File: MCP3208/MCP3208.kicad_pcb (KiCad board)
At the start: 2 copper layers, 52.3 x 29.7 mm, 34 parts, among them J1 5V, J2 SPI, J3 CH4, J4 CH3, J5 CH2, J6 CH1, U1 MCP1541, U2 MCP6021, U3 MCP3208

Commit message: PCB layout changes
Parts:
- moved C8 0.80 mm to (108.0, 79.4)
- moved J1 0.64 mm to (127.3, 66.7)
- moved J2 0.64 mm to (127.3, 72.9)
- moved C2 0.25 mm to (117.0, 63.5)
- moved FB1 0.25 mm to (106.3, 66.9)
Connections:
- U2 pad 1: Net-(U2-Pad1) -> (no net)
- U2 pad 5: Net-(U2-Pad5) -> (no net)
- U2 pad 8: Net-(U2-Pad8) -> (no net)
- U3 pad 6: Net-(U3-Pad6) -> (no net)
- U3 pad 7: Net-(U3-Pad7) -> (no net)
- U3 pad 8: Net-(U3-Pad8) -> (no net)
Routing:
- net GND: track 50.8 -> 53.2 mm, vias 19 -> 23
- net /SPI.MISO: track 24.3 -> 25.2 mm
- net /SPI.MOSI: track 23.8 -> 24.7 mm
- net /SPI.CS0: track 23.2 -> 24.2 mm
- net /SPI.CLK: track 24.8 -> 25.8 mm
- net Net-(C8-Pad2): track 13.3 -> 13.9 mm

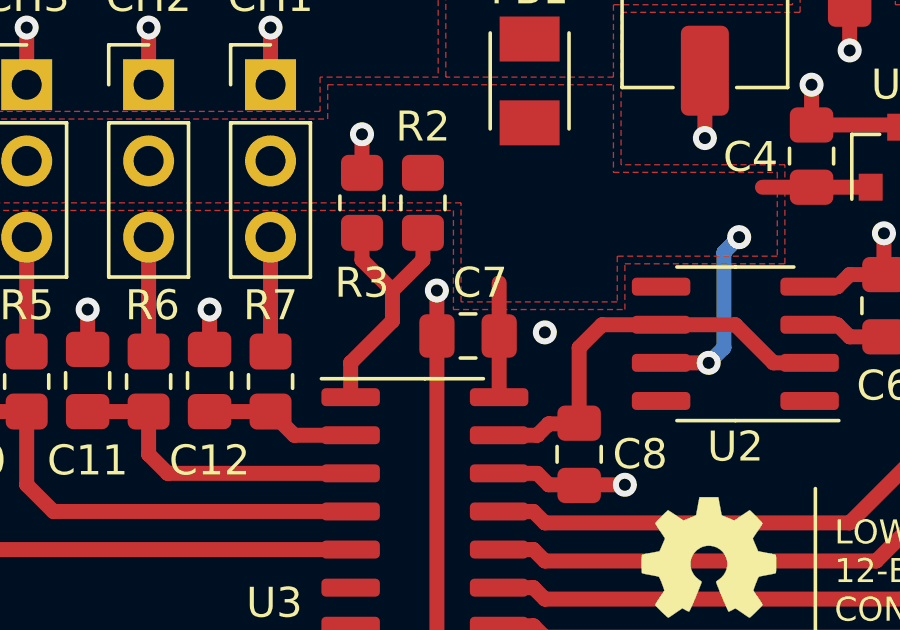
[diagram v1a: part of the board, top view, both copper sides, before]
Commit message: Changes to schematic layout
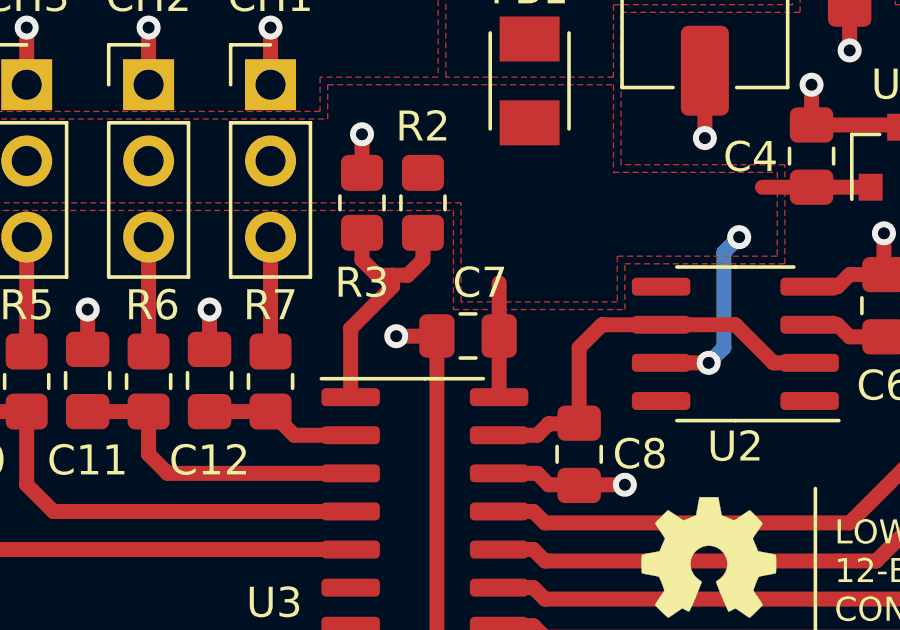
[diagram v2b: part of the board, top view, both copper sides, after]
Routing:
- net GND: track 53.2 -> 53.0 mm, vias 23 -> 22

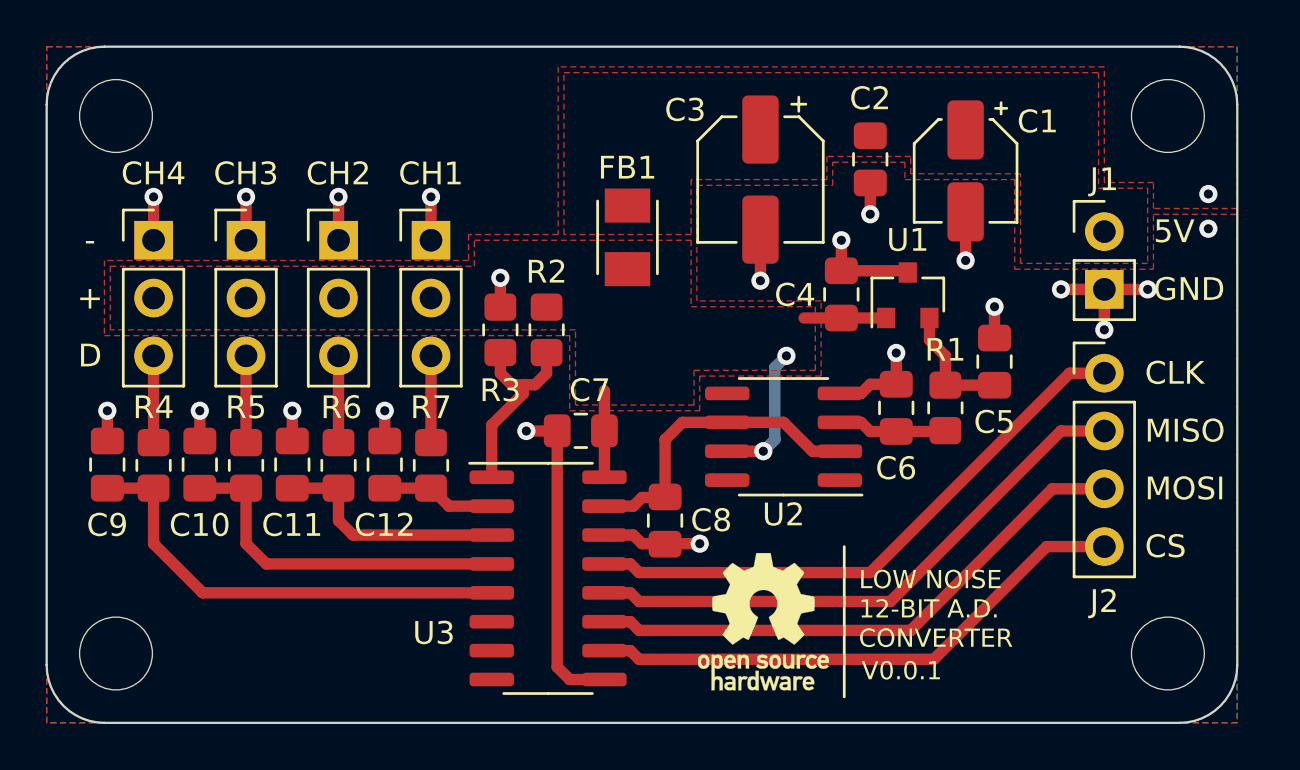
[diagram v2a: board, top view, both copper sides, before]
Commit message: Changes to footprints
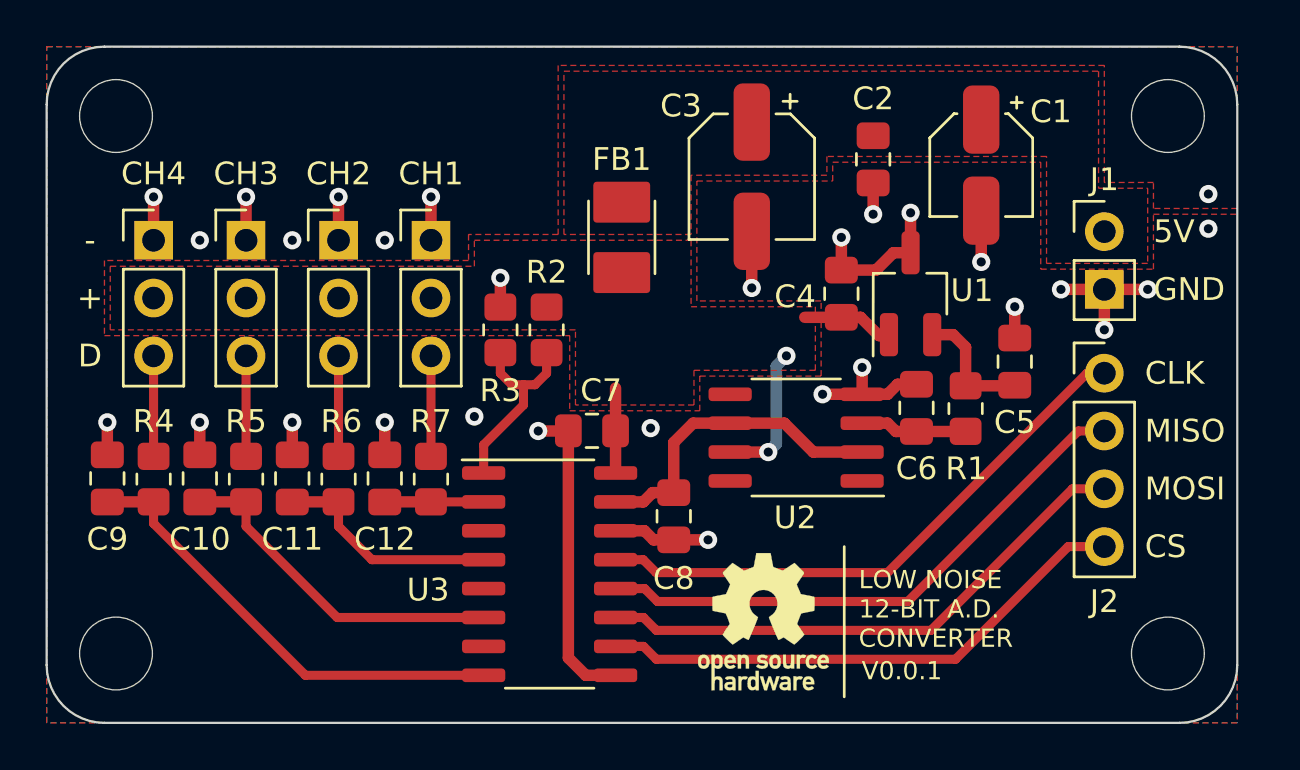
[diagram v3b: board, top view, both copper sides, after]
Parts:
- C1: footprint Capacitor_SMD:CP_Elec_4x4.5 -> Capacitor_SMD:CP_Elec_4x4.5_HandSolder
- C3: footprint Capacitor_SMD:CP_Elec_5x5.3 -> Capacitor_SMD:CP_Elec_5x5.3_HandSolder
- FB1: footprint Ferrite_THT:FIL_NFZ32BW210HN11L -> Ferrite_THT:FIL_NFZ32BW210HN11L_HandSolder
- U1: footprint Package_TO_SOT_SMD:SOT-23 -> Package_TO_SOT_SMD:SOT-23_Handsoldering_MCP
- U2: footprint Package_SO:SOIC-8_3.9x4.9mm_P1.27mm -> Package_SO:SOIC-8_MCP_HandSolder
- U3: footprint Package_SO:SOIC-16_3.9x9.9mm_P1.27mm -> Package_SO:SOIC-16_MCP_HandSolder
- moved R1 0.89 mm to (121.2, 74.5)
- moved C5 0.89 mm to (123.3, 72.4)
- moved C6 0.89 mm to (119.0, 74.4)
- moved C1 0.73 mm to (121.8, 63.8)
- moved C10 0.61 mm to (87.5, 77.5)
- moved C11 0.61 mm to (91.6, 77.5)
- moved C12 0.61 mm to (95.6, 77.5)
- moved C9 0.61 mm to (83.4, 77.5)
- moved R7 0.60 mm to (97.7, 77.6)
- moved R4 0.60 mm to (85.5, 77.6)
- moved R5 0.60 mm to (89.5, 77.6)
- moved R6 0.60 mm to (93.6, 77.6)
- moved U3 0.58 mm to (103.3, 81.5)
- moved U2 0.57 mm to (113.7, 75.9)
- moved C7 0.49 mm to (104.7, 75.4)
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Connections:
- net Net-(C12-Pad2) renamed CH.1
- net Net-(R2-Pad2) renamed CH.0
- C10 pad 2: Net-(C10-Pad2) -> CH.3
- C11 pad 2: Net-(C11-Pad2) -> CH.2
- C9 pad 2: Net-(C9-Pad2) -> CH.4
- R4 pad 2: Net-(C9-Pad2) -> CH.4
- R5 pad 2: Net-(C10-Pad2) -> CH.3
- R6 pad 2: Net-(C11-Pad2) -> CH.2
- U3 pad 3: Net-(C11-Pad2) -> Net-(U3-Pad3)
- U3 pad 4: Net-(C10-Pad2) -> CH.2
- U3 pad 5: Net-(C9-Pad2) -> Net-(U3-Pad5)
- U3 pad 6: (no net) -> CH.3
- U3 pad 7: (no net) -> Net-(U3-Pad7)
- U3 pad 8: (no net) -> CH.4
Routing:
- net CH.4: track 0.00 -> 20.3 mm
- net Net-(C9-Pad2): track 20.2 -> 0.00 mm
- net Net-(C10-Pad2): track 15.6 -> 0.00 mm
- net CH.3: track 0.00 -> 15.2 mm
- net Net-(C11-Pad2): track 10.5 -> 0.00 mm
- net CH.2: track 0.00 -> 10.1 mm
- net GND: track 53.0 -> 57.5 mm, vias 22 -> 29
- net CH.1: track 5.03 -> 4.35 mm
- net Net-(J6-Pad3): track 3.81 -> 4.42 mm
- net Net-(J5-Pad3): track 3.81 -> 4.42 mm
- net Net-(J4-Pad3): track 3.81 -> 4.42 mm
- net Net-(J3-Pad3): track 3.81 -> 4.42 mm
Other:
- net class Power added: clearance 0.25, trace_width 0.504, via_dia 0.8, via_drill 0.4
- net class Signal added: clearance 0.25, trace_width 0.4, via_dia 0.8, via_drill 0.4
